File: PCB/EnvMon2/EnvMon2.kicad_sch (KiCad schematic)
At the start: 37 parts, among them J1 USB-C, J2 DC, J3 TEMP, J4 Shelly, M1 OLED1.5-RGB, SW1 SW_Push, SW2 SW_Push, SW3 SW_Push, U1 LMR16006+FB, U2 SCD41, U3 FT231XQ, U4 ESP32-PICO-MINI-02, U5 QR, U6 VEML3235SL-RA

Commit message: Library update
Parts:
- removed D3: RGB, RevK:LED-RGB-1.6x1.6, symbol Device:LED_ARGB
- added D3: LED_BARG, RevK:MHS190RGBCT, symbol Device:LED_BARG
- C1: footprint RevK:C_0603_ -> RevK:Hidden; LCSC Part # (none) -> C30926
- C2: footprint RevK:C_0805_ -> RevK:Hidden; LCSC Part # (none) -> C19110
- C3: footprint RevK:C_0805_ -> RevK:Hidden; LCSC Part # (none) -> C17024
- D1: footprint RevK:D_1206_ -> RevK:Hidden; JLCPCB Rotation Offset (none) -> 180; LCSC Part # (none) -> C143805; Part No CD1206-B2100 -> (none)
- J1: LCSC Part # (none) -> C709357
- L1: footprint RevK:L_4x4_ -> RevK:Hidden; LCSC Part # (none) -> C354575; Manufacturer Laird -> (none); Part No TYA4020 -> (none)
- R1: value 100k 1% or 0R -> 100k 1%; LCSC Part # (none) -> C14675
- R2: value 30k 1% or NF -> 30k 1%; LCSC Part # (none) -> C100001
- U1: value LMR16006+FB -> LMR16006XDDCR; footprint RevK:RegulatorBlockFB -> RevK:SOT-23-Thin-6-Reg; LCSC Part # (none) -> C87080
- U3: footprint RevK:QFN-20-1EP_4x4mm_P0.5mm_EP2.5x2.5mm -> RevK:JLC-QFN-20-1EP_4x4mm_P0.5mm_EP2.5x2.5m
- U4: LCSC Part # (none) -> C2980306; Part No (none) -> ESP32-PICO-MINI-02-N8R2
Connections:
- net B: now also U4.33 (IO19); no longer U4.28 (IO8)
- net G: now also U4.27 (IO7); no longer U4.33 (IO19)
- net R: now also U4.28 (IO8); no longer U4.27 (IO7)
- net at R9.1: now also D3.1 (BK)
- net at R7.1: now also D3.3 (RK)
- net at R8.1: now also D3.4 (GK)
- net +3V3 renamed +3.3V
- net +3.3V: now also D3.2 (A)
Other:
- moved on the sheet: J4

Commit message: Revised production files
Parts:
- removed U6: VEML3235SL-RA, RevK:VEML3235SL-RA, symbol RevK:VEML3235SL
- added U6: VEML3235SL_RA, RevK:VEML3235SL-RA, symbol RevK:VEML3235SL_RA
- C1: footprint RevK:Hidden -> RevK:C_0603_
- C2, C3: footprint RevK:Hidden -> RevK:C_0805_
- D1: footprint RevK:Hidden -> RevK:D_1206_; JLCPCB Rotation Offset 180 -> (none)
- D2: LCSC Part # (none) -> C143805
- L1: footprint RevK:Hidden -> RevK:L_4x4_
- U1: Manufacturer TI -> (none); Part No LMR16006YQ3 -> (none)
- U3: footprint RevK:JLC-QFN-20-1EP_4x4mm_P0.5mm_EP2.5x2.5m -> RevK:QFN-20-1EP_4x4mm_P0.5mm_EP2.5x2.5mm; JLCPCB Rotation Offset (none) -> -90
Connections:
- net +3.3V: now also U6.1 (VDD)
- net GND: now also U6.2 (GND)
- net SCL: now also U6.4 (SCL)
- net SDA: now also U6.3 (SDA)

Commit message: Production file update
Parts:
- removed U1: LMR16006XDDCR, RevK:SOT-23-Thin-6-Reg, symbol RevK:LMR16006+FB
- added U1: LMR16006XDDCR, RevK:SOT-23-Thin-6-Reg, symbol RevK:LMR16006XDDCR
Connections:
- net +3.3V: now also U1.7 (VOUT)
- net DC: now also U1.4 (SHDN), U1.5 (VIN)
- net GND: now also U1.2 (GND)
- net at R1.2, R2.2: now also U1.3 (FB)
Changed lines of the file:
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@@
   (junction (at 226.06 52.07) (diameter 0) (color 0 0 0 0)
   )
+  (junction (at 49.53 142.24) (diameter 0) (color 0 0 0 0)
+  )
   (junction (at 160.02 58.42) (diameter 0) (color 0 0 0 0)
-  )
-  (junction (at 49.53 142.24) (diameter 0) (color 0 0 0 0)
   )
   (junction (at 38.1 133.35) (diameter 0) (color 0 0 0 0)
@@
     (pin "1")
     (pin "2")
+  )
+  (symbol (lib_id "RevK:LMR16006XDDCR") (at 49.53 132.08 0) (unit 1)
+    (in_bom yes) (on_board yes) (fields_autoplaced)
+    (property "Reference" "U1" (id 0) (at 67.31 127.2372 0))
+    (property "Value" "LMR16006XDDCR" (id 1) (at 67.31 129.7741 0))
+    (property "Footprint" "RevK:SOT-23-Thin-6-Reg" (id 2) (at 64.77 148.59 0)
+      (effects (font (size 1.27 1.27)) hide)
+    )
+    (property "Datasheet" "" (id 3) (at 60.96 129.54 0)
+      (effects (font (size 1.27 1.27)) hide)
+    )
+    (property "Manufacturer" "TI" (id 4) (at 77.47 146.685 0)
+      (effects (font (size 1.27 1.27)) hide)
+    )
+    (property "Part No" "LMR16006XDDCR" (id 5) (at 67.945 146.685 0)
+      (effects (font (size 1.27 1.27)) hide)
+    )
+    (property "LCSC Part #" "C87080" (id 6) (at 55.245 146.685 0)
+      (effects (font (size 1.27 1.27)) hide)
+    )
+    (property "JLCPCB Rotation Offset" "90" (id 7) (at 80.01 146.685 0)
+      (effects (font (size 1.27 1.27)) hide)
+    )
+    (pin "1")
+    (pin "2")
+    (pin "3")
+    (pin "4")
+    (pin "5")
+    (pin "6")
+    (pin "7")
   )
   (symbol (lib_id "power:+3.3V") (at 198.12 137.16 90) (unit 1)
@@
     (pin "2")
   )
-  (symbol (lib_id "RevK:LMR16006+FB") (at 49.53 132.08 0) (unit 1)
-    (in_bom yes) (on_board yes) (fields_autoplaced)
-    (property "Reference" "U1" (id 0) (at 83.185 136.3253 0)
-      (effects (font (size 1.27 1.27)) (justify left))
-    )
-    (property "Value" "LMR16006XDDCR" (id 1) (at 83.185 138.8622 0)
-      (effects (font (size 1.27 1.27)) (justify left))
-    )
-    (property "Footprint" "RevK:SOT-23-Thin-6-Reg" (id 2) (at 60.96 129.54 0)
-      (effects (font (size 1.27 1.27)) hide)
-    )
-    (property "Datasheet" "~" (id 3) (at 60.96 129.54 0)
-      (effects (font (size 1.27 1.27)) hide)
-    )
-    (property "LCSC Part #" "C87080" (id 4) (at 49.53 132.08 0)
-      (effects (font (size 1.27 1.27)) hide)
-    )
-    (pin "1")
-    (pin "2")
-    (pin "3")
-    (pin "4")
-    (pin "5")
-  )
   (symbol (lib_id "RevK:AJK") (at 276.86 170.18 0) (unit 1)
     (in_bom no) (on_board yes)
@@
       (reference "SW3") (unit 1) (value "SW_Push") (footprint "Button_Switch_THT:SW_PUSH_6mm_H13mm")
     )
-    (path "/9b557f0a-725f-4242-b7e7-d2c14325285b"
+    (path "/49fac067-22c4-46c0-be10-03a6c28d472f"
       (reference "U1") (unit 1) (value "LMR16006XDDCR") (footprint "RevK:SOT-23-Thin-6-Reg")
     )

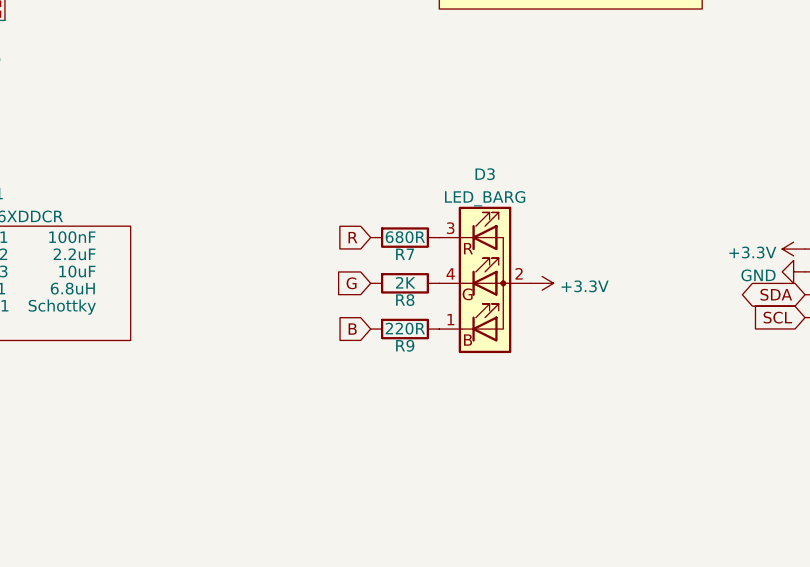
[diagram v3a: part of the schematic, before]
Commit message: Resistor update for LED
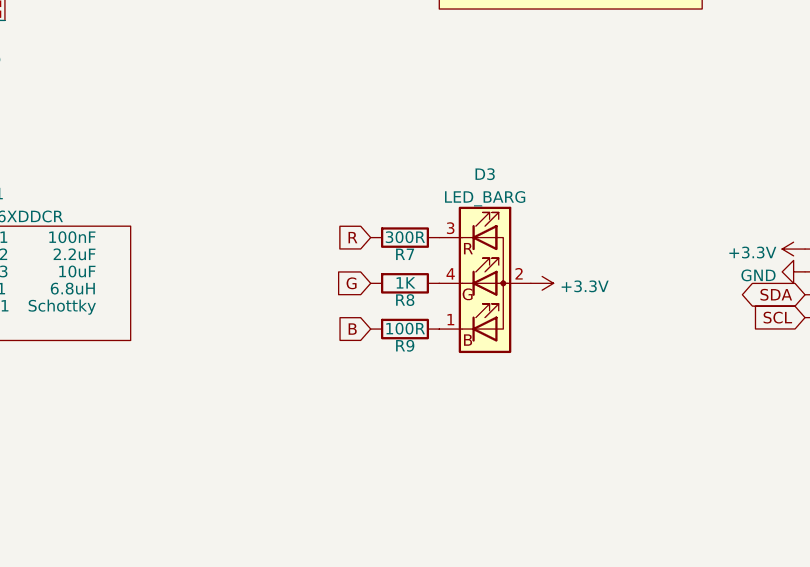
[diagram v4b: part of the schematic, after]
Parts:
- R7: value 680R -> 300R
- R8: value 2K -> 1K
- R9: value 220R -> 100R
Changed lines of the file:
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@@
     (in_bom yes) (on_board yes)
     (property "Reference" "R9" (id 0) (at 113.03 144.145 90))
-    (property "Value" "220R" (id 1) (at 113.03 142.24 90))
+    (property "Value" "100R" (id 1) (at 113.03 142.24 90))
     (property "Footprint" "RevK:R_0603" (id 2) (at 113.03 140.462 90)
       (effects (font (size 1.27 1.27)) hide)
@@
     (in_bom yes) (on_board yes)
     (property "Reference" "R7" (id 0) (at 113.03 133.985 90))
-    (property "Value" "680R" (id 1) (at 113.03 132.08 90))
+    (property "Value" "300R" (id 1) (at 113.03 132.08 90))
     (property "Footprint" "RevK:R_0603" (id 2) (at 113.03 130.302 90)
       (effects (font (size 1.27 1.27)) hide)
@@
     (in_bom yes) (on_board yes)
     (property "Reference" "R8" (id 0) (at 113.03 139.065 90))
-    (property "Value" "2K" (id 1) (at 113.03 137.16 90))
+    (property "Value" "1K" (id 1) (at 113.03 137.16 90))
     (property "Footprint" "RevK:R_0603" (id 2) (at 113.03 135.382 90)
       (effects (font (size 1.27 1.27)) hide)
@@
     )
     (path "/00000000-0000-0000-0000-000060cf9e4d"
-      (reference "R7") (unit 1) (value "680R") (footprint "RevK:R_0603")
+      (reference "R7") (unit 1) (value "300R") (footprint "RevK:R_0603")
     )
     (path "/00000000-0000-0000-0000-000060cfbfaf"
-      (reference "R8") (unit 1) (value "2K") (footprint "RevK:R_0603")
+      (reference "R8") (unit 1) (value "1K") (footprint "RevK:R_0603")
     )
     (path "/00000000-0000-0000-0000-000060a436c8"
-      (reference "R9") (unit 1) (value "220R") (footprint "RevK:R_0603")
+      (reference "R9") (unit 1) (value "100R") (footprint "RevK:R_0603")
     )
     (path "/e7149988-8da9-4254-8dc1-168b761f2899"

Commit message: Extra diode
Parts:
- added D4: D, RevK:D_1206, symbol Device:D
- J3: now in the parts list
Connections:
- net DC: now also D4.1 (K); no longer J2.2 (DC)
- new net: D4.2 (A), J2.2 (DC)
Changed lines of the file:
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@@
     )
   )
-  (global_label "DC" (shape output) (at 48.26 123.825 180) (fields_autoplaced)
+  (global_label "DC" (shape output) (at 40.64 123.825 180) (fields_autoplaced)
     (effects (font (size 1.27 1.27)) (justify right))
-    (property "Intersheet References" "${INTERSHEET_REFS}" (id 0) (at 281.94 152.4 0)
+    (property "Intersheet References" "${INTERSHEET_REFS}" (id 0) (at 274.32 152.4 0)
       (effects (font (size 1.27 1.27)) hide)
     )
@@
   )
   (symbol (lib_id "Connector_Generic:Conn_01x03") (at 203.2 134.62 0) (unit 1)
-    (in_bom no) (on_board yes) (fields_autoplaced)
+    (in_bom yes) (on_board yes) (fields_autoplaced)
     (property "Reference" "J3" (id 0) (at 205.232 133.7853 0)
       (effects (font (size 1.27 1.27)) (justify left))
@@
     )
     (pin "1")
+  )
+  (symbol (lib_id "Device:D") (at 44.45 123.825 0) (unit 1)
+    (in_bom yes) (on_board yes)
+    (property "Reference" "D4" (id 0) (at 44.45 129.3368 0))
+    (property "Value" "D" (id 1) (at 44.45 127.0254 0))
+    (property "Footprint" "RevK:D_1206" (id 2) (at 44.45 123.825 0)
+      (effects (font (size 1.27 1.27)) hide)
+    )
+    (property "Datasheet" "~" (id 3) (at 44.45 123.825 0)
+      (effects (font (size 1.27 1.27)) hide)
+    )
+    (property "LCSC Part #" "C143805" (id 4) (at 44.45 123.825 0)
+      (effects (font (size 1.27 1.27)) hide)
+    )
+    (pin "1")
+    (pin "2")
   )
   (symbol (lib_id "Device:R") (at 196.85 124.46 90) (unit 1)
@@
       (reference "D3") (unit 1) (value "LED_BARG") (footprint "RevK:MHS190RGBCT")
     )
+    (path "/3d4a7dd0-fbca-4010-8c9c-eea6a8f33171"
+      (reference "D4") (unit 1) (value "D") (footprint "RevK:D_1206")
+    )
     (path "/00000000-0000-0000-0000-0000604764e2"
